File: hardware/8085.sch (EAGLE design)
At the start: 52 parts, among them IC10 74HCT00N, IC11 74HCT245DW, IC2 74AC573N, IC3 ATF16V8BP3, IC4 74AC00D, IC5 74HCT245DW, IC6 74AC273N, IC7 74HCT139N, IC8 7404N, IC9 74HCT138N

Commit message: Bug in PCB design fixed
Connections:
- net CF_CS0: now also IC11A.G
- net GND: now also IC3.GND, IC3.I2, IC3.I7, IC3.I8
- net IO_RD: now also IC11A.DIR
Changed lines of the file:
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@@
 <part name="C8" library="rcl" deviceset="C-EU" device="C0603" value="22p"/>
 <part name="GND17" library="supply1" deviceset="GND" device=""/>
+<part name="GND18" library="supply1" deviceset="GND" device=""/>
 </parts>
 <sheets>
@@
 <instance part="C8" gate="G$1" x="-25.4" y="2.54" rot="R90"/>
 <instance part="GND17" gate="1" x="-30.48" y="-2.54"/>
+<instance part="GND18" gate="1" x="45.72" y="-111.76"/>
 </instances>
 <busses>
@@
 <wire x1="-30.48" y1="2.54" x2="-30.48" y2="0" width="0.1524" layer="91"/>
 </segment>
+<segment>
+<pinref part="IC3" gate="G$1" pin="GND"/>
+<pinref part="GND18" gate="1" pin="GND"/>
+<wire x1="48.26" y1="-106.68" x2="45.72" y2="-106.68" width="0.1524" layer="91"/>
+<wire x1="45.72" y1="-106.68" x2="45.72" y2="-109.22" width="0.1524" layer="91"/>
+<pinref part="IC3" gate="G$1" pin="I8"/>
+<wire x1="48.26" y1="-101.6" x2="45.72" y2="-101.6" width="0.1524" layer="91"/>
+<wire x1="45.72" y1="-101.6" x2="45.72" y2="-106.68" width="0.1524" layer="91"/>
+<junction x="45.72" y="-106.68"/>
+<pinref part="IC3" gate="G$1" pin="I7"/>
+<wire x1="48.26" y1="-99.06" x2="45.72" y2="-99.06" width="0.1524" layer="91"/>
+<wire x1="45.72" y1="-99.06" x2="45.72" y2="-101.6" width="0.1524" layer="91"/>
+<junction x="45.72" y="-101.6"/>
+<pinref part="IC3" gate="G$1" pin="I2"/>
+<wire x1="48.26" y1="-86.36" x2="45.72" y2="-86.36" width="0.1524" layer="91"/>
+<wire x1="45.72" y1="-86.36" x2="45.72" y2="-99.06" width="0.1524" layer="91"/>
+<junction x="45.72" y="-99.06"/>
+</segment>
 </net>
 <net name="D0" class="0">
@@
 <label x="200.66" y="-289.56" size="1.4224" layer="95" rot="R180" xref="yes"/>
 </segment>
+<segment>
+<pinref part="IC11" gate="A" pin="DIR"/>
+<wire x1="106.68" y1="-320.04" x2="111.76" y2="-320.04" width="0.1524" layer="91"/>
+</segment>
 </net>
 <net name="RESET" class="0">
@@
 <pinref part="IC6" gate="A" pin="CLK"/>
 <wire x1="332.74" y1="-30.48" x2="325.12" y2="-30.48" width="0.1524" layer="91"/>
+<label x="325.12" y="-30.48" size="1.4224" layer="95" rot="R180" xref="yes"/>
 </segment>
 <segment>
@@
 <wire x1="68.58" y1="-96.52" x2="76.2" y2="-96.52" width="0.1524" layer="91"/>
 </segment>
-</net>
+<segment>
+<pinref part="IC11" gate="A" pin="G"/>
+<wire x1="106.68" y1="-322.58" x2="111.76" y2="-322.58" width="0.1524" layer="91"/>
+</segment>
+</net>

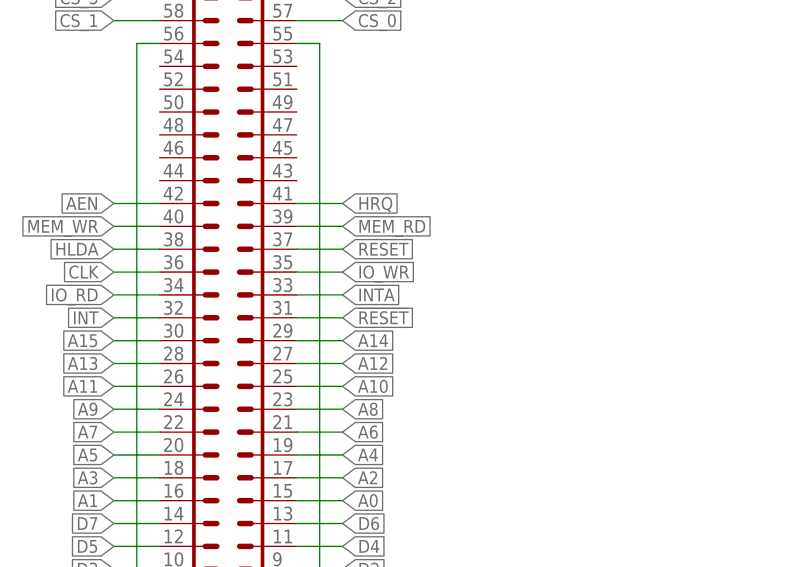
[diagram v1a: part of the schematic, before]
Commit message: Bug in PCB board design fixed
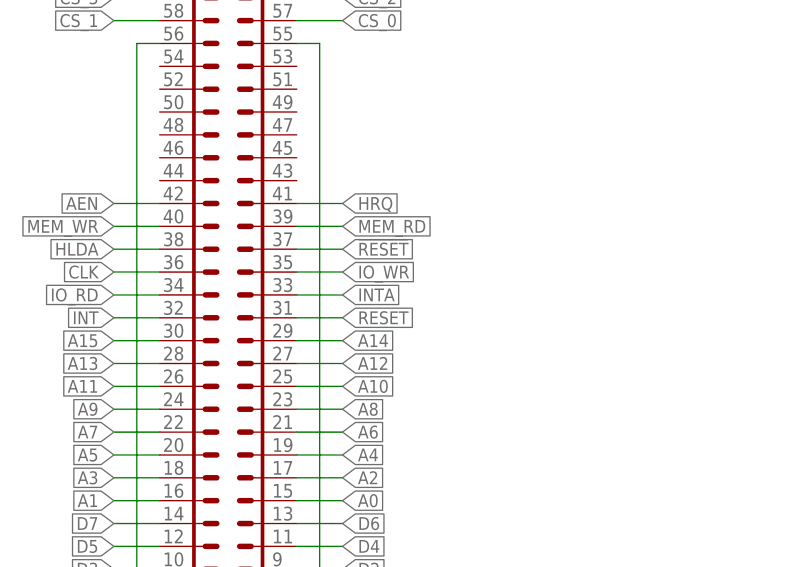
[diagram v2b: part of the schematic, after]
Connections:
- net !RESET: now also SV2.37; no longer SV2.31
- net RESET: now also SV2.31; no longer SV2.37
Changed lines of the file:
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@@
 <net name="!RESET" class="0">
-<segment>
-<wire x1="160.02" y1="-33.02" x2="165.1" y2="-33.02" width="0.1524" layer="91"/>
-<label x="165.1" y="-33.02" size="1.4224" layer="95" xref="yes"/>
-<pinref part="SV2" gate="1" pin="31"/>
-</segment>
 <segment>
 <pinref part="IC6" gate="A" pin="CLR"/>
@@
 <wire x1="205.74" y1="-299.72" x2="200.66" y2="-299.72" width="0.1524" layer="91"/>
 <label x="200.66" y="-299.72" size="1.4224" layer="95" rot="R180" xref="yes"/>
+</segment>
+<segment>
+<wire x1="160.02" y1="-25.4" x2="165.1" y2="-25.4" width="0.1524" layer="91"/>
+<label x="165.1" y="-25.4" size="1.4224" layer="95" xref="yes"/>
+<pinref part="SV2" gate="1" pin="37"/>
 </segment>
 </net>
@@
 <net name="RESET" class="0">
 <segment>
-<wire x1="160.02" y1="-25.4" x2="165.1" y2="-25.4" width="0.1524" layer="91"/>
-<label x="165.1" y="-25.4" size="1.4224" layer="95" xref="yes"/>
-<pinref part="SV2" gate="1" pin="37"/>
-</segment>
-<segment>
 <pinref part="IC1" gate="G$1" pin="RES_OUT"/>
 <wire x1="25.4" y1="-10.16" x2="30.48" y2="-10.16" width="0.1524" layer="91"/>
@@
 <pinref part="IC8" gate="B" pin="I"/>
 </segment>
-</net>
+<segment>
+<wire x1="160.02" y1="-33.02" x2="165.1" y2="-33.02" width="0.1524" layer="91"/>
+<label x="165.1" y="-33.02" size="1.4224" layer="95" xref="yes"/>
+<pinref part="SV2" gate="1" pin="31"/>
+</segment>
+</net>

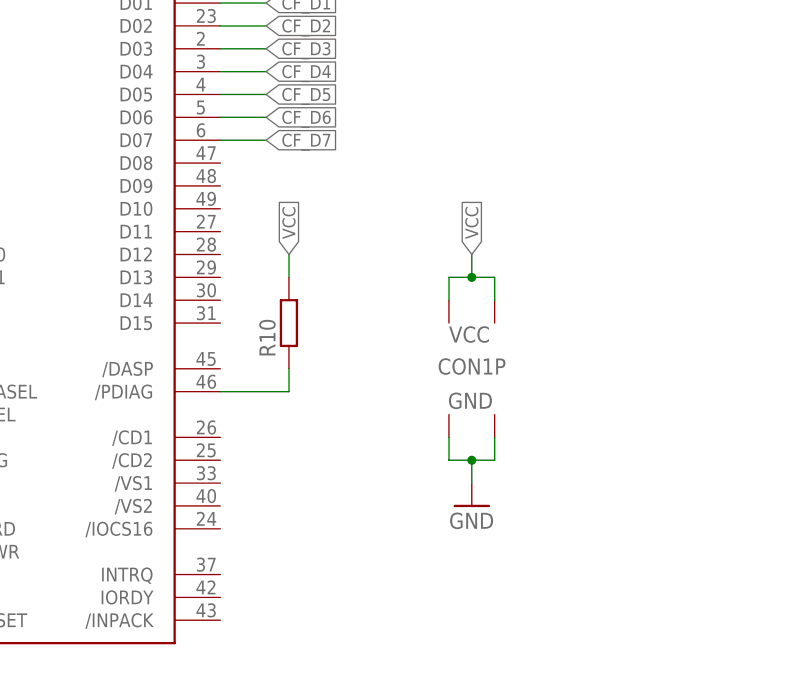
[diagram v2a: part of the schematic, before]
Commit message: CF indicator LED added to CPU board
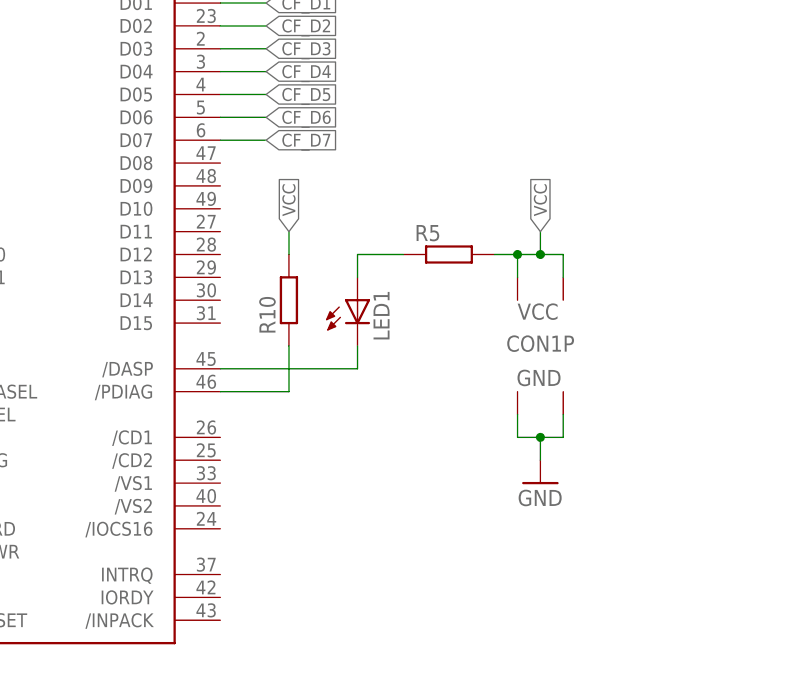
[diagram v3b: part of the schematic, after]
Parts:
- added LED1: (no value), led:LED5MM
- added R5: (no value), rcl:R-EU_M1206
- R10, R8: device rcl:R-EU_0207/10 -> rcl:R-EU_0207/12
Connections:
- new net N$15: LED1.A, R5.1
- new net N$16: CON1G$1./DASP, LED1.C
- net VCC: now also R5.2
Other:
- moved on the sheet: CON1P, R10
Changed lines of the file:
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@@
 <part name="GND20" library="supply1" deviceset="GND" device=""/>
 <part name="R7" library="rcl" deviceset="R-EU_" device="0207/10"/>
-<part name="R8" library="rcl" deviceset="R-EU_" device="0207/10"/>
-<part name="R10" library="rcl" deviceset="R-EU_" device="0207/10"/>
+<part name="R8" library="rcl" deviceset="R-EU_" device="0207/12"/>
+<part name="R10" library="rcl" deviceset="R-EU_" device="0207/12"/>
 <part name="R11" library="rcl" deviceset="R-EU_" device="0207/10"/>
 <part name="RN1" library="resistor-sil" deviceset="G04R" device=""/>
@@
 <part name="GND17" library="supply1" deviceset="GND" device=""/>
 <part name="GND18" library="supply1" deviceset="GND" device=""/>
+<part name="R5" library="rcl" deviceset="R-EU_" device="M1206"/>
+<part name="LED1" library="led" deviceset="LED" device="5MM"/>
 </parts>
 <sheets>
@@
 <instance part="CON1" gate="G$1" x="223.52" y="-264.16"/>
 <instance part="GND19" gate="1" x="203.2" y="-307.34"/>
-<instance part="CON1" gate="P" x="269.24" y="-271.78"/>
-<instance part="GND20" gate="1" x="269.24" y="-287.02"/>
+<instance part="CON1" gate="P" x="276.86" y="-269.24"/>
+<instance part="GND20" gate="1" x="276.86" y="-284.48"/>
 <instance part="R7" gate="G$1" x="185.42" y="-269.24" rot="R90"/>
 <instance part="R8" gate="G$1" x="190.5" y="-269.24" rot="R90"/>
-<instance part="R10" gate="G$1" x="248.92" y="-266.7" rot="R90"/>
+<instance part="R10" gate="G$1" x="248.92" y="-264.16" rot="R90"/>
 <instance part="R11" gate="G$1" x="195.58" y="-254" rot="R90"/>
 <instance part="RN1" gate="A" x="-33.02" y="40.64"/>
@@
 <instance part="GND17" gate="1" x="-30.48" y="-2.54"/>
 <instance part="GND18" gate="1" x="45.72" y="-111.76"/>
+<instance part="R5" gate="G$1" x="266.7" y="-259.08"/>
+<instance part="LED1" gate="G$1" x="256.54" y="-264.16"/>
 </instances>
 <busses>
@@
 <segment>
 <pinref part="CON1" gate="P" pin="VCC1"/>
-<wire x1="266.7" y1="-264.16" x2="266.7" y2="-261.62" width="0.1524" layer="91"/>
+<wire x1="274.32" y1="-261.62" x2="274.32" y2="-259.08" width="0.1524" layer="91"/>
 <pinref part="CON1" gate="P" pin="VCC2"/>
-<wire x1="266.7" y1="-261.62" x2="269.24" y2="-261.62" width="0.1524" layer="91"/>
-<wire x1="269.24" y1="-261.62" x2="271.78" y2="-261.62" width="0.1524" layer="91"/>
-<wire x1="271.78" y1="-261.62" x2="271.78" y2="-264.16" width="0.1524" layer="91"/>
-<wire x1="269.24" y1="-261.62" x2="269.24" y2="-259.08" width="0.1524" layer="91"/>
-<junction x="269.24" y="-261.62"/>
-<label x="269.24" y="-259.08" size="1.4224" layer="95" rot="R90" xref="yes"/>
+<wire x1="274.32" y1="-259.08" x2="276.86" y2="-259.08" width="0.1524" layer="91"/>
+<wire x1="276.86" y1="-259.08" x2="279.4" y2="-259.08" width="0.1524" layer="91"/>
+<wire x1="279.4" y1="-259.08" x2="279.4" y2="-261.62" width="0.1524" layer="91"/>
+<wire x1="276.86" y1="-259.08" x2="276.86" y2="-256.54" width="0.1524" layer="91"/>
+<junction x="276.86" y="-259.08"/>
+<label x="276.86" y="-256.54" size="1.4224" layer="95" rot="R90" xref="yes"/>
+<pinref part="R5" gate="G$1" pin="2"/>
+<wire x1="274.32" y1="-259.08" x2="271.78" y2="-259.08" width="0.1524" layer="91"/>
+<junction x="274.32" y="-259.08"/>
 </segment>
 <segment>
@@
 <segment>
 <pinref part="R10" gate="G$1" pin="2"/>
-<wire x1="248.92" y1="-261.62" x2="248.92" y2="-259.08" width="0.1524" layer="91"/>
-<label x="248.92" y="-259.08" size="1.4224" layer="95" rot="R90" xref="yes"/>
+<wire x1="248.92" y1="-259.08" x2="248.92" y2="-256.54" width="0.1524" layer="91"/>
+<label x="248.92" y="-256.54" size="1.4224" layer="95" rot="R90" xref="yes"/>
 </segment>
 <segment>
@@
 <segment>
 <pinref part="CON1" gate="P" pin="GND1"/>
-<wire x1="266.7" y1="-279.4" x2="266.7" y2="-281.94" width="0.1524" layer="91"/>
+<wire x1="274.32" y1="-276.86" x2="274.32" y2="-279.4" width="0.1524" layer="91"/>
 <pinref part="CON1" gate="P" pin="GND2"/>
-<wire x1="266.7" y1="-281.94" x2="269.24" y2="-281.94" width="0.1524" layer="91"/>
-<wire x1="269.24" y1="-281.94" x2="271.78" y2="-281.94" width="0.1524" layer="91"/>
-<wire x1="271.78" y1="-281.94" x2="271.78" y2="-279.4" width="0.1524" layer="91"/>
+<wire x1="274.32" y1="-279.4" x2="276.86" y2="-279.4" width="0.1524" layer="91"/>
+<wire x1="276.86" y1="-279.4" x2="279.4" y2="-279.4" width="0.1524" layer="91"/>
+<wire x1="279.4" y1="-279.4" x2="279.4" y2="-276.86" width="0.1524" layer="91"/>
 <pinref part="GND20" gate="1" pin="GND"/>
-<wire x1="269.24" y1="-284.48" x2="269.24" y2="-281.94" width="0.1524" layer="91"/>
-<junction x="269.24" y="-281.94"/>
+<wire x1="276.86" y1="-281.94" x2="276.86" y2="-279.4" width="0.1524" layer="91"/>
+<junction x="276.86" y="-279.4"/>
 </segment>
 <segment>
@@
 <pinref part="R10" gate="G$1" pin="1"/>
 <wire x1="241.3" y1="-274.32" x2="248.92" y2="-274.32" width="0.1524" layer="91"/>
-<wire x1="248.92" y1="-274.32" x2="248.92" y2="-271.78" width="0.1524" layer="91"/>
+<wire x1="248.92" y1="-274.32" x2="248.92" y2="-269.24" width="0.1524" layer="91"/>
 </segment>
 </net>
@@
 </segment>
 </net>
+<net name="N$15" class="0">
+<segment>
+<pinref part="R5" gate="G$1" pin="1"/>
+<pinref part="LED1" gate="G$1" pin="A"/>
+<wire x1="261.62" y1="-259.08" x2="256.54" y2="-259.08" width="0.1524" layer="91"/>
+<wire x1="256.54" y1="-259.08" x2="256.54" y2="-261.62" width="0.1524" layer="91"/>
+</segment>
+</net>
+<net name="N$16" class="0">
+<segment>
+<pinref part="CON1" gate="G$1" pin="/DASP"/>
+<pinref part="LED1" gate="G$1" pin="C"/>
+<wire x1="241.3" y1="-271.78" x2="256.54" y2="-271.78" width="0.1524" layer="91"/>
+<wire x1="256.54" y1="-271.78" x2="256.54" y2="-269.24" width="0.1524" layer="91"/>
+</segment>
+</net>

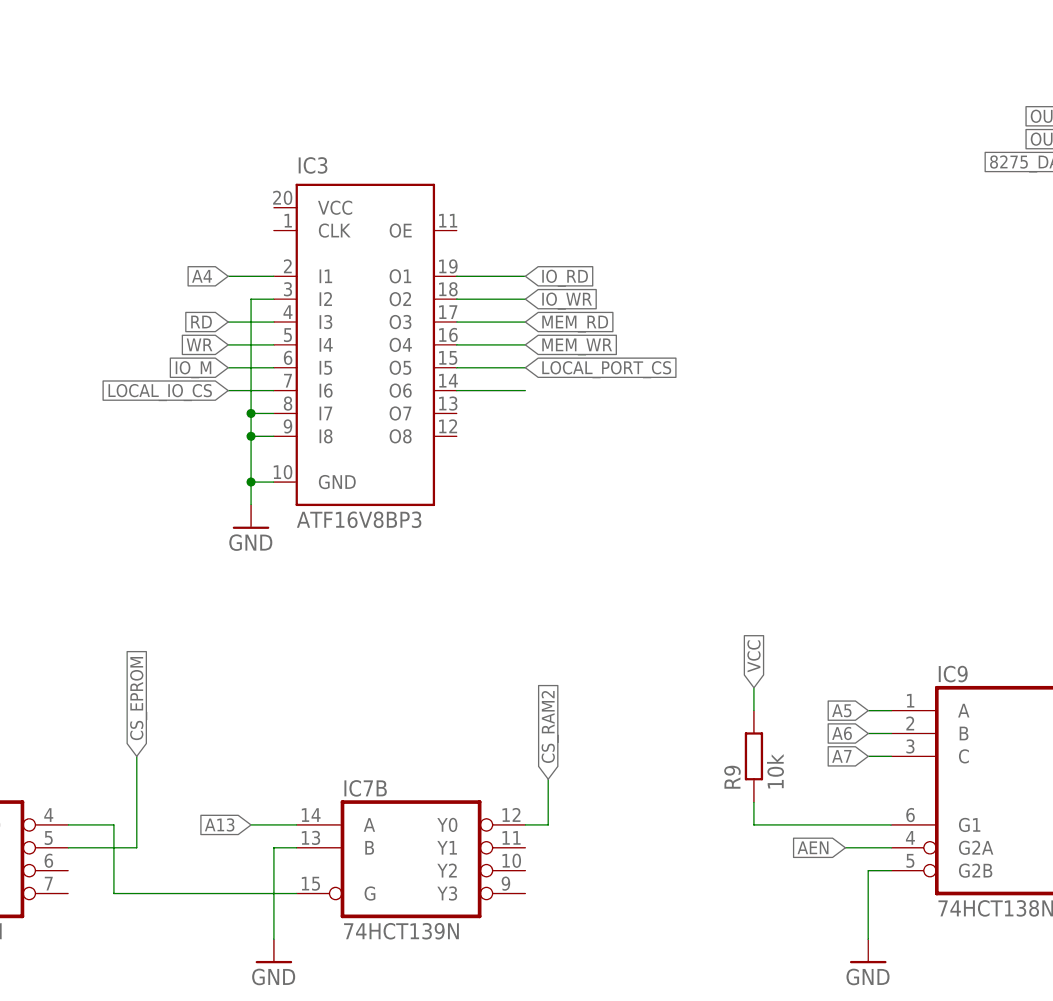
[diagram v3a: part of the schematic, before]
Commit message: IO address decoder gated with IOM signal
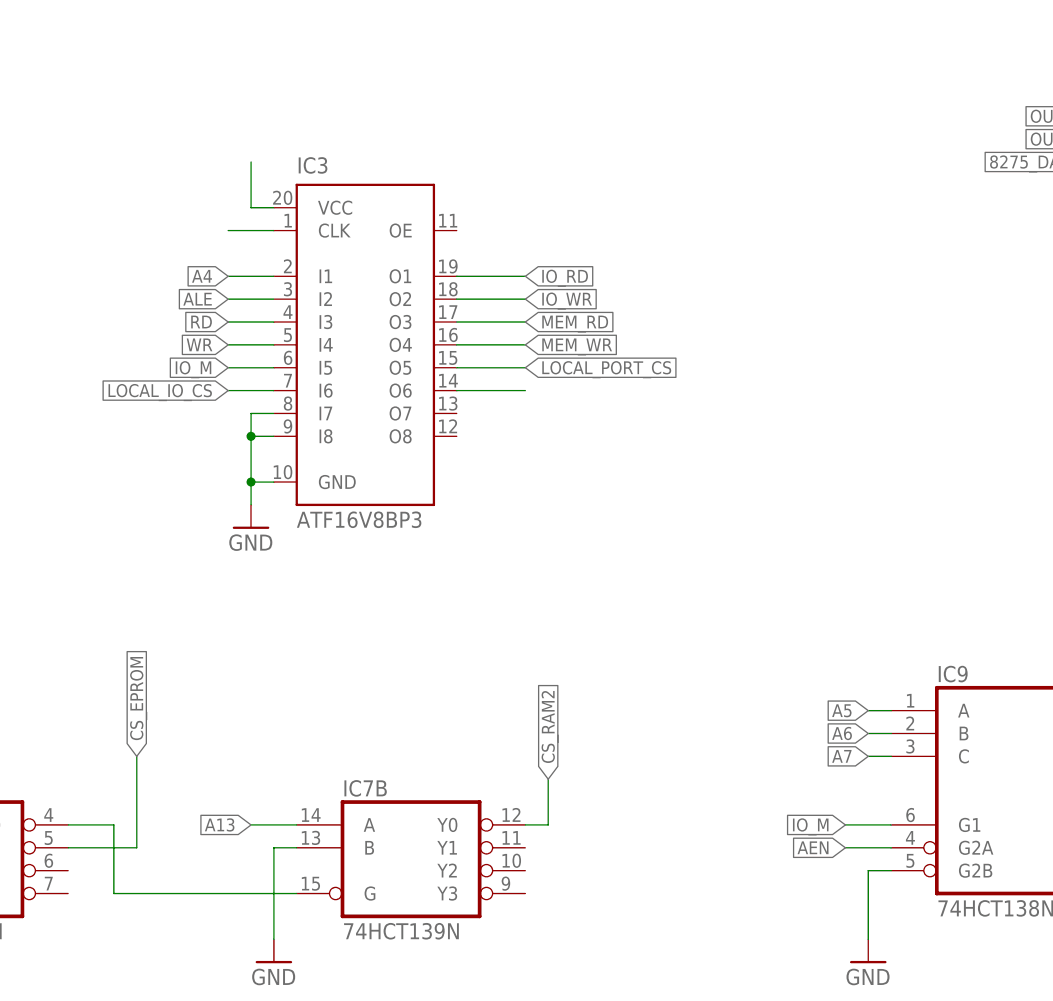
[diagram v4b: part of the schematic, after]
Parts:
- removed R9: 10k, rcl:R-EU_M1206
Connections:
- removed net N$20: IC9A.G1, R9.1
- net ALE: now also IC3.I2
- net CLK: now also IC3.CLK
- net GND: no longer IC3.I2
- net IO_M: now also IC9A.G1
- net VCC: now also IC3.VCC; no longer R9.2
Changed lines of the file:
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@@
 <part name="C9" library="rcl" deviceset="C-EU" device="C1206" value="100n"/>
 <part name="GND12" library="supply1" deviceset="GND" device=""/>
-<part name="R9" library="rcl" deviceset="R-EU_" device="M1206" value="10k"/>
 <part name="C10" library="rcl" deviceset="CPOL-EU" device="E5-10.5"/>
 <part name="C11" library="rcl" deviceset="C-EU" device="C0805" value="100n"/>
@@
 <instance part="C9" gate="G$1" x="167.64" y="137.16"/>
 <instance part="GND12" gate="1" x="114.3" y="-160.02"/>
-<instance part="R9" gate="G$1" x="101.6" y="-137.16" rot="R90"/>
 <instance part="C10" gate="G$1" x="121.92" y="137.16"/>
 <instance part="C11" gate="G$1" x="175.26" y="137.16"/>
@@
 </segment>
 <segment>
-<pinref part="R9" gate="G$1" pin="2"/>
-<wire x1="101.6" y1="-132.08" x2="101.6" y2="-129.54" width="0.1524" layer="91"/>
-<label x="101.6" y="-129.54" size="1.4224" layer="95" rot="R90" xref="yes"/>
-</segment>
-<segment>
 <pinref part="IC9" gate="P" pin="VCC"/>
 <wire x1="312.42" y1="144.78" x2="312.42" y2="149.86" width="0.1524" layer="91"/>
@@
 <junction x="228.6" y="142.24"/>
 </segment>
+<segment>
+<pinref part="IC3" gate="G$1" pin="VCC"/>
+<wire x1="48.26" y1="-76.2" x2="45.72" y2="-76.2" width="0.1524" layer="91"/>
+<wire x1="45.72" y1="-76.2" x2="45.72" y2="-71.12" width="0.1524" layer="91"/>
+</segment>
 </net>
 <net name="GND" class="0">
@@
 <wire x1="45.72" y1="-99.06" x2="45.72" y2="-101.6" width="0.1524" layer="91"/>
 <junction x="45.72" y="-101.6"/>
-<pinref part="IC3" gate="G$1" pin="I2"/>
-<wire x1="48.26" y1="-86.36" x2="45.72" y2="-86.36" width="0.1524" layer="91"/>
-<wire x1="45.72" y1="-86.36" x2="45.72" y2="-99.06" width="0.1524" layer="91"/>
-<junction x="45.72" y="-99.06"/>
 </segment>
 </net>
@@
 <wire x1="25.4" y1="-17.78" x2="33.02" y2="-17.78" width="0.1524" layer="91"/>
 <label x="33.02" y="-17.78" size="1.4224" layer="95" xref="yes"/>
+</segment>
+<segment>
+<pinref part="IC3" gate="G$1" pin="CLK"/>
+<wire x1="48.26" y1="-78.74" x2="43.18" y2="-78.74" width="0.1524" layer="91"/>
 </segment>
 </net>
@@
 </segment>
 </net>
-<net name="N$20" class="0">
-<segment>
-<pinref part="IC9" gate="A" pin="G1"/>
-<wire x1="116.84" y1="-144.78" x2="101.6" y2="-144.78" width="0.1524" layer="91"/>
-<pinref part="R9" gate="G$1" pin="1"/>
-<wire x1="101.6" y1="-144.78" x2="101.6" y2="-142.24" width="0.1524" layer="91"/>
-</segment>
-</net>
 <net name="OUT_4" class="0">
 <segment>
@@
 <wire x1="-2.54" y1="119.38" x2="-7.62" y2="119.38" width="0.1524" layer="91"/>
 <label x="-7.62" y="119.38" size="1.4224" layer="95" rot="R180" xref="yes"/>
+</segment>
+<segment>
+<pinref part="IC3" gate="G$1" pin="I2"/>
+<wire x1="48.26" y1="-86.36" x2="43.18" y2="-86.36" width="0.1524" layer="91"/>
+<label x="43.18" y="-86.36" size="1.4224" layer="95" rot="R180" xref="yes"/>
 </segment>
 </net>
@@
 <label x="43.18" y="-93.98" size="1.4224" layer="95" rot="R180" xref="yes"/>
 </segment>
-</net>
+<segment>
+<pinref part="IC9" gate="A" pin="G1"/>
+<wire x1="116.84" y1="-144.78" x2="111.76" y2="-144.78" width="0.1524" layer="91"/>
+<label x="111.76" y="-144.78" size="1.4224" layer="95" rot="R180" xref="yes"/>
+</segment>
+</net>

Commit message: Another minor PCB update
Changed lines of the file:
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@@
 <pinref part="IC8" gate="P" pin="VCC"/>
 <wire x1="-22.86" y1="-251.46" x2="-22.86" y2="-243.84" width="0.1524" layer="91"/>
+<label x="-22.86" y="-243.84" size="1.4224" layer="95" rot="R90" xref="yes"/>
 </segment>
 <segment>
@@
 <wire x1="48.26" y1="-76.2" x2="45.72" y2="-76.2" width="0.1524" layer="91"/>
 <wire x1="45.72" y1="-76.2" x2="45.72" y2="-71.12" width="0.1524" layer="91"/>
+<label x="45.72" y="-71.12" size="1.4224" layer="95" rot="R90" xref="yes"/>
 </segment>
 </net>
@@
 <pinref part="IC3" gate="G$1" pin="CLK"/>
 <wire x1="48.26" y1="-78.74" x2="43.18" y2="-78.74" width="0.1524" layer="91"/>
+<label x="43.18" y="-78.74" size="1.4224" layer="95" rot="R180" xref="yes"/>
 </segment>
 </net>
@@
 <pinref part="IC3" gate="G$1" pin="O6"/>
 <wire x1="68.58" y1="-96.52" x2="76.2" y2="-96.52" width="0.1524" layer="91"/>
-</segment>
-<segment>
+<label x="76.2" y="-96.52" size="1.4224" layer="95" xref="yes"/>
+</segment>
+<segment>
